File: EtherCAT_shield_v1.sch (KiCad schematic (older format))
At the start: 3 parts

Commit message: 配線
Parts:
- added C1: 0.1u, symbol C
- added C2, C3: 0.022u, symbol C
- added D1, D2: LED, symbol LED
- added P1: CONN_02X10, symbol CONN_02X10
- added P2, P3: CONN_02X19, symbol CONN_02X19
- added R1: 10k, symbol R
- added R2: 0R, symbol R
- added R3, R5: 330, symbol R
- added R4: 0, symbol R
- added R6, R7: R, symbol R
- gave numbers to parts that had none: 3
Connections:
- net labels added: +3V3, +5V
- wire segments 0 -> 146
- no-connect marks 1 -> 10
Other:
- moved on the sheet: J1, J2

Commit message: 部品修正．一度アノテーションとネットリスト生成
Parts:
- removed U1: LAN9252, symbol LAN9252
- added U1: LAN9252, Housings_DFN_QFN:QFN-64-1EP_9x9mm_Pitch0.5mm, symbol LAN9252
- C1, C2, C3: footprint (none) -> Capacitors_SMD:C_0603
- D1, D2: footprint (none) -> LEDs:LED_0603
- J1, J2: footprint (none) -> Connect:RJHSE538X
- P1: footprint (none) -> Socket_Strips:Socket_Strip_Straight_2x10_Pitch2.54mm
- P2, P3: footprint (none) -> Pin_Headers:Pin_Header_Straight_2x19_Pitch2.54mm
- R1: renamed from R6; footprint (none) -> Resistors_SMD:R_0603
- R2: renamed from R7; footprint (none) -> Resistors_SMD:R_0603
- R3: renamed from R2; footprint (none) -> Resistors_SMD:R_0603
- R4: renamed from R1; footprint (none) -> Resistors_SMD:R_0603
- R5: renamed from R3; footprint (none) -> Resistors_SMD:R_0603
- R6: renamed from R4; footprint (none) -> Resistors_SMD:R_0603
- R7: renamed from R5; footprint (none) -> Resistors_SMD:R_0603
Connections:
- wire segments 146 -> 138

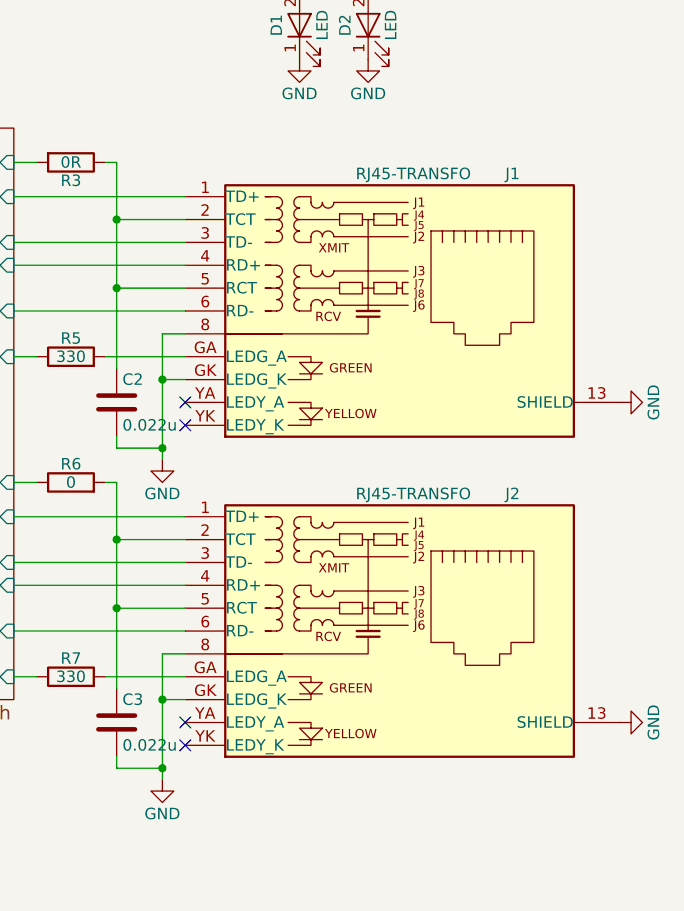
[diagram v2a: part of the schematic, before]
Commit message: 部品変更，再アノテーション，コネクタだけ配置
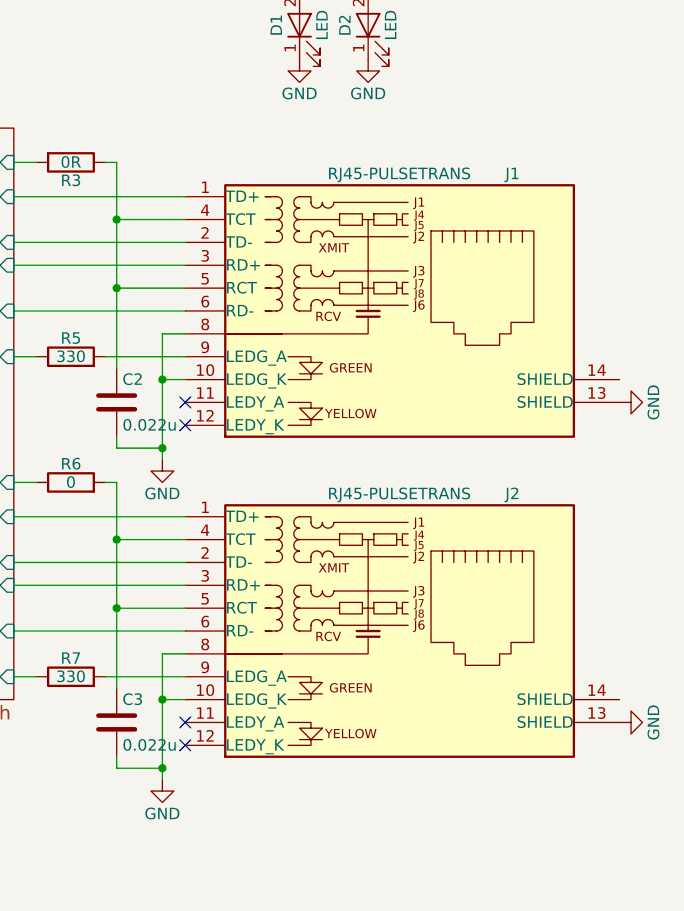
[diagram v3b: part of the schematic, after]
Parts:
- removed J1, J2: RJ45-TRANSFO, Connect:RJHSE538X, symbol RJ45-TRANSFO
- added J1, J2: RJ45-PULSETRANS, Connect:RJ45_J0011D21BNL, symbol RJ45-PULSETRANS
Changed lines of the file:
@@
 EESchema Schematic File Version 2
-LIBS:EtherCAT_shield_v1-rescue
 LIBS:power
 LIBS:device
@@
 $EndSheet
 $Comp
-L GND #PWR01
+L GND #PWR9
 U 1 1 58D8F78B
 P 10350 3150
-F 0 "#PWR01" H 10350 2900 50  0001 C CNN
+F 0 "#PWR9" H 10350 2900 50  0001 C CNN
 F 1 "GND" H 10350 3000 50  0000 C CNN
 F 2 "" H 10350 3150 50  0000 C CNN
@@
 $EndComp
 $Comp
-L GND #PWR02
+L GND #PWR13
 U 1 1 58D8F7A6
 P 10350 4550
-F 0 "#PWR02" H 10350 4300 50  0001 C CNN
+F 0 "#PWR13" H 10350 4300 50  0001 C CNN
 F 1 "GND" H 10350 4400 50  0000 C CNN
 F 2 "" H 10350 4550 50  0000 C CNN
@@
 	7700 2950 7800 2950
 $Comp
-L GND #PWR03
+L GND #PWR10
 U 1 1 58D9CD09
 P 8350 3400
-F 0 "#PWR03" H 8350 3150 50  0001 C CNN
+F 0 "#PWR10" H 8350 3150 50  0001 C CNN
 F 1 "GND" H 8350 3250 50  0000 C CNN
 F 2 "" H 8350 3400 50  0000 C CNN
@@
 Connection ~ 8350 4450
 $Comp
-L GND #PWR04
+L GND #PWR14
 U 1 1 58DAC772
 P 8350 4800
-F 0 "#PWR04" H 8350 4550 50  0001 C CNN
+F 0 "#PWR14" H 8350 4550 50  0001 C CNN
 F 1 "GND" H 8350 4650 50  0000 C CNN
 F 2 "" H 8350 4800 50  0000 C CNN
@@
 $EndComp
 $Comp
-L +3V3 #PWR05
+L +3V3 #PWR1
 U 1 1 58DDD983
 P 8950 1050
-F 0 "#PWR05" H 8950 900 50  0001 C CNN
+F 0 "#PWR1" H 8950 900 50  0001 C CNN
 F 1 "+3V3" H 8950 1190 50  0000 C CNN
 F 2 "" H 8950 1050 50  0000 C CNN
@@
 $EndComp
 $Comp
-L GND #PWR06
+L GND #PWR3
 U 1 1 58DDE236
 P 8950 1650
-F 0 "#PWR06" H 8950 1400 50  0001 C CNN
+F 0 "#PWR3" H 8950 1400 50  0001 C CNN
 F 1 "GND" H 8950 1500 50  0000 C CNN
 F 2 "" H 8950 1650 50  0000 C CNN
@@
 $EndComp
 $Comp
-L GND #PWR07
+L GND #PWR18
 U 1 1 58DE40E7
 P 3300 6100
-F 0 "#PWR07" H 3300 5850 50  0001 C CNN
+F 0 "#PWR18" H 3300 5850 50  0001 C CNN
 F 1 "GND" H 3300 5950 50  0000 C CNN
 F 2 "" H 3300 6100 50  0000 C CNN
@@
 $EndComp
 $Comp
-L GND #PWR08
+L GND #PWR15
 U 1 1 58DE4A0C
 P 3800 5500
-F 0 "#PWR08" H 3800 5250 50  0001 C CNN
+F 0 "#PWR15" H 3800 5250 50  0001 C CNN
 F 1 "GND" H 3800 5350 50  0000 C CNN
 F 2 "" H 3800 5500 50  0000 C CNN
@@
 $EndComp
 $Comp
-L GND #PWR09
+L GND #PWR19
 U 1 1 58DE5361
 P 3900 6100
-F 0 "#PWR09" H 3900 5850 50  0001 C CNN
+F 0 "#PWR19" H 3900 5850 50  0001 C CNN
 F 1 "GND" H 3900 5950 50  0000 C CNN
 F 2 "" H 3900 6100 50  0000 C CNN
@@
 Connection ~ 3850 6100
 $Comp
-L +3V3 #PWR010
+L +3V3 #PWR17
 U 1 1 58DE575E
 P 3950 5800
-F 0 "#PWR010" H 3950 5650 50  0001 C CNN
+F 0 "#PWR17" H 3950 5650 50  0001 C CNN
 F 1 "+3V3" H 3950 5940 50  0000 C CNN
 F 2 "" H 3950 5800 50  0000 C CNN
@@
 NoConn ~ 3300 5500
 $Comp
-L GND #PWR011
+L GND #PWR21
 U 1 1 58DE7D3E
 P 5950 6700
-F 0 "#PWR011" H 5950 6450 50  0001 C CNN
+F 0 "#PWR21" H 5950 6450 50  0001 C CNN
 F 1 "GND" H 5950 6550 50  0000 C CNN
 F 2 "" H 5950 6700 50  0000 C CNN
@@
 $EndComp
 $Comp
-L GND #PWR012
+L GND #PWR20
 U 1 1 58DE8701
 P 5950 6100
-F 0 "#PWR012" H 5950 5850 50  0001 C CNN
+F 0 "#PWR20" H 5950 5850 50  0001 C CNN
 F 1 "GND" H 5950 5950 50  0000 C CNN
 F 2 "" H 5950 6100 50  0000 C CNN
@@
 $EndComp
 $Comp
-L GND #PWR013
+L GND #PWR16
 U 1 1 58DE8FB1
 P 5450 5600
-F 0 "#PWR013" H 5450 5350 50  0001 C CNN
+F 0 "#PWR16" H 5450 5350 50  0001 C CNN
 F 1 "GND" H 5450 5450 50  0000 C CNN
 F 2 "" H 5450 5600 50  0000 C CNN
@@
 	2650 3300 2200 3300
 $Comp
-L GND #PWR014
+L GND #PWR12
 U 1 1 58DF79D7
 P 2200 3500
-F 0 "#PWR014" H 2200 3250 50  0001 C CNN
+F 0 "#PWR12" H 2200 3250 50  0001 C CNN
 F 1 "GND" H 2200 3350 50  0000 C CNN
 F 2 "" H 2200 3500 50  0000 C CNN
@@
 $EndComp
 $Comp
-L GND #PWR015
+L GND #PWR11
 U 1 1 58DF80F0
 P 1700 3500
-F 0 "#PWR015" H 1700 3250 50  0001 C CNN
+F 0 "#PWR11" H 1700 3250 50  0001 C CNN
 F 1 "GND" H 1700 3350 50  0000 C CNN
 F 2 "" H 1700 3500 50  0000 C CNN
@@
 	1650 2600 1650 2250
 $Comp
-L +3V3 #PWR016
+L +3V3 #PWR5
 U 1 1 58E0E7BC
 P 1650 2250
-F 0 "#PWR016" H 1650 2100 50  0001 C CNN
+F 0 "#PWR5" H 1650 2100 50  0001 C CNN
 F 1 "+3V3" H 1650 2390 50  0000 C CNN
 F 2 "" H 1650 2250 50  0000 C CNN
@@
 $EndComp
 $Comp
-L +5V #PWR017
+L +5V #PWR6
 U 1 1 58E0EC99
 P 2250 2250
-F 0 "#PWR017" H 2250 2100 50  0001 C CNN
+F 0 "#PWR6" H 2250 2100 50  0001 C CNN
 F 1 "+5V" H 2250 2390 50  0000 C CNN
 F 2 "" H 2250 2250 50  0000 C CNN
@@
 $EndComp
 $Comp
-L GND #PWR018
+L GND #PWR4
 U 1 1 58E0FDD7
 P 9250 1650
-F 0 "#PWR018" H 9250 1400 50  0001 C CNN
+F 0 "#PWR4" H 9250 1400 50  0001 C CNN
 F 1 "GND" H 9250 1500 50  0000 C CNN
 F 2 "" H 9250 1650 50  0000 C CNN
@@
 $EndComp
 $Comp
-L +5V #PWR019
+L +5V #PWR2
 U 1 1 58E10702
 P 9250 1050
-F 0 "#PWR019" H 9250 900 50  0001 C CNN
+F 0 "#PWR2" H 9250 900 50  0001 C CNN
 F 1 "+5V" H 9250 1190 50  0000 C CNN
 F 2 "" H 9250 1050 50  0000 C CNN
@@
 NoConn ~ 3300 4050
 $Comp
-L +3V3 #PWR020
+L +3V3 #PWR7
 U 1 1 58E1F1DF
 P 6500 2350
-F 0 "#PWR020" H 6500 2200 50  0001 C CNN
+F 0 "#PWR7" H 6500 2200 50  0001 C CNN
 F 1 "+3V3" H 6500 2490 50  0000 C CNN
 F 2 "" H 6500 2350 50  0000 C CNN
@@
 $EndComp
 $Comp
-L GND #PWR021
+L GND #PWR8
 U 1 1 58E20E63
 P 6500 3050
-F 0 "#PWR021" H 6500 2800 50  0001 C CNN
+F 0 "#PWR8" H 6500 2800 50  0001 C CNN
 F 1 "GND" H 6500 2900 50  0000 C CNN
 F 2 "" H 6500 3050 50  0000 C CNN
@@
 	3900 5800 3950 5800
 Connection ~ 3900 5800
-$Comp
-L RJ45-TRANSFO J1
-U 1 1 58D9E482
-P 9750 2750
-F 0 "J1" H 9850 3350 50  0000 L CNN
-F 1 "RJ45-TRANSFO" H 9700 3350 50  0000 R CNN
-F 2 "Connect:RJHSE538X" H 9750 2750 50  0001 C CNN
-F 3 "" H 9750 2750 50  0001 C CNN
-	1    9750 2750
-	1    0    0    -1
-$EndComp
-$Comp
-L RJ45-TRANSFO J2
-U 1 1 58D9F003
-P 9750 4150
-F 0 "J2" H 9850 4750 50  0000 L CNN
-F 1 "RJ45-TRANSFO" H 9700 4750 50  0000 R CNN
-F 2 "Connect:RJHSE538X" H 9750 4150 50  0001 C CNN
-F 3 "" H 9750 4150 50  0001 C CNN
-	1    9750 4150
-	1    0    0    -1
-$EndComp
 Wire Wire Line
 	8450 3750 8150 3750
@@
 	-1   0    0    -1
 $EndComp
+$Comp
+L RJ45-PULSETRANS J1
+U 1 1 58DA5610
+P 9750 2750
+F 0 "J1" H 9850 3350 50  0000 L CNN
+F 1 "RJ45-PULSETRANS" H 9700 3350 50  0000 R CNN
+F 2 "Connect:RJ45_J0011D21BNL" H 9750 2750 50  0001 C CNN
+F 3 "" H 9750 2750 50  0001 C CNN
+	1    9750 2750
+	1    0    0    -1
+$EndComp
+$Comp
+L RJ45-PULSETRANS J2
+U 1 1 58DA58D5
+P 9750 4150
+F 0 "J2" H 9850 4750 50  0000 L CNN
+F 1 "RJ45-PULSETRANS" H 9700 4750 50  0000 R CNN
+F 2 "Connect:RJ45_J0011D21BNL" H 9750 4150 50  0001 C CNN
+F 3 "" H 9750 4150 50  0001 C CNN
+	1    9750 4150
+	1    0    0    -1
+$EndComp
 $EndSCHEMATC

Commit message: 進捗
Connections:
- net labels added: RX1_N, RX1_P, RX2_N, RX2_P, TX1_N, TX1_P, TX2_N, TX2_P
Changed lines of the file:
@@
 $EndSheet
 $Comp
-L GND #PWR9
+L GND #PWR01
 U 1 1 58D8F78B
 P 10350 3150
-F 0 "#PWR9" H 10350 2900 50  0001 C CNN
+F 0 "#PWR01" H 10350 2900 50  0001 C CNN
 F 1 "GND" H 10350 3000 50  0000 C CNN
 F 2 "" H 10350 3150 50  0000 C CNN
@@
 $EndComp
 $Comp
-L GND #PWR13
+L GND #PWR02
 U 1 1 58D8F7A6
 P 10350 4550
-F 0 "#PWR13" H 10350 4300 50  0001 C CNN
+F 0 "#PWR02" H 10350 4300 50  0001 C CNN
 F 1 "GND" H 10350 4400 50  0000 C CNN
 F 2 "" H 10350 4550 50  0000 C CNN
@@
 	7700 2950 7800 2950
 $Comp
-L GND #PWR10
+L GND #PWR03
 U 1 1 58D9CD09
 P 8350 3400
-F 0 "#PWR10" H 8350 3150 50  0001 C CNN
+F 0 "#PWR03" H 8350 3150 50  0001 C CNN
 F 1 "GND" H 8350 3250 50  0000 C CNN
 F 2 "" H 8350 3400 50  0000 C CNN
@@
 Connection ~ 8350 4450
 $Comp
-L GND #PWR14
+L GND #PWR04
 U 1 1 58DAC772
 P 8350 4800
-F 0 "#PWR14" H 8350 4550 50  0001 C CNN
+F 0 "#PWR04" H 8350 4550 50  0001 C CNN
 F 1 "GND" H 8350 4650 50  0000 C CNN
 F 2 "" H 8350 4800 50  0000 C CNN
@@
 $EndComp
 $Comp
-L +3V3 #PWR1
+L +3V3 #PWR05
 U 1 1 58DDD983
 P 8950 1050
-F 0 "#PWR1" H 8950 900 50  0001 C CNN
+F 0 "#PWR05" H 8950 900 50  0001 C CNN
 F 1 "+3V3" H 8950 1190 50  0000 C CNN
 F 2 "" H 8950 1050 50  0000 C CNN
@@
 $EndComp
 $Comp
-L GND #PWR3
+L GND #PWR06
 U 1 1 58DDE236
 P 8950 1650
-F 0 "#PWR3" H 8950 1400 50  0001 C CNN
+F 0 "#PWR06" H 8950 1400 50  0001 C CNN
 F 1 "GND" H 8950 1500 50  0000 C CNN
 F 2 "" H 8950 1650 50  0000 C CNN
@@
 $EndComp
 $Comp
-L GND #PWR18
+L GND #PWR07
 U 1 1 58DE40E7
 P 3300 6100
-F 0 "#PWR18" H 3300 5850 50  0001 C CNN
+F 0 "#PWR07" H 3300 5850 50  0001 C CNN
 F 1 "GND" H 3300 5950 50  0000 C CNN
 F 2 "" H 3300 6100 50  0000 C CNN
@@
 $EndComp
 $Comp
-L GND #PWR15
+L GND #PWR08
 U 1 1 58DE4A0C
 P 3800 5500
-F 0 "#PWR15" H 3800 5250 50  0001 C CNN
+F 0 "#PWR08" H 3800 5250 50  0001 C CNN
 F 1 "GND" H 3800 5350 50  0000 C CNN
 F 2 "" H 3800 5500 50  0000 C CNN
@@
 $EndComp
 $Comp
-L GND #PWR19
+L GND #PWR09
 U 1 1 58DE5361
 P 3900 6100
-F 0 "#PWR19" H 3900 5850 50  0001 C CNN
+F 0 "#PWR09" H 3900 5850 50  0001 C CNN
 F 1 "GND" H 3900 5950 50  0000 C CNN
 F 2 "" H 3900 6100 50  0000 C CNN
@@
 Connection ~ 3850 6100
 $Comp
-L +3V3 #PWR17
+L +3V3 #PWR010
 U 1 1 58DE575E
 P 3950 5800
-F 0 "#PWR17" H 3950 5650 50  0001 C CNN
+F 0 "#PWR010" H 3950 5650 50  0001 C CNN
 F 1 "+3V3" H 3950 5940 50  0000 C CNN
 F 2 "" H 3950 5800 50  0000 C CNN
@@
 NoConn ~ 3300 5500
 $Comp
-L GND #PWR21
+L GND #PWR011
 U 1 1 58DE7D3E
 P 5950 6700
-F 0 "#PWR21" H 5950 6450 50  0001 C CNN
+F 0 "#PWR011" H 5950 6450 50  0001 C CNN
 F 1 "GND" H 5950 6550 50  0000 C CNN
 F 2 "" H 5950 6700 50  0000 C CNN
@@
 $EndComp
 $Comp
-L GND #PWR20
+L GND #PWR012
 U 1 1 58DE8701
 P 5950 6100
-F 0 "#PWR20" H 5950 5850 50  0001 C CNN
+F 0 "#PWR012" H 5950 5850 50  0001 C CNN
 F 1 "GND" H 5950 5950 50  0000 C CNN
 F 2 "" H 5950 6100 50  0000 C CNN
@@
 $EndComp
 $Comp
-L GND #PWR16
+L GND #PWR013
 U 1 1 58DE8FB1
 P 5450 5600
-F 0 "#PWR16" H 5450 5350 50  0001 C CNN
+F 0 "#PWR013" H 5450 5350 50  0001 C CNN
 F 1 "GND" H 5450 5450 50  0000 C CNN
 F 2 "" H 5450 5600 50  0000 C CNN
@@
 	2650 3300 2200 3300
 $Comp
-L GND #PWR12
+L GND #PWR014
 U 1 1 58DF79D7
 P 2200 3500
-F 0 "#PWR12" H 2200 3250 50  0001 C CNN
+F 0 "#PWR014" H 2200 3250 50  0001 C CNN
 F 1 "GND" H 2200 3350 50  0000 C CNN
 F 2 "" H 2200 3500 50  0000 C CNN
@@
 $EndComp
 $Comp
-L GND #PWR11
+L GND #PWR015
 U 1 1 58DF80F0
 P 1700 3500
-F 0 "#PWR11" H 1700 3250 50  0001 C CNN
+F 0 "#PWR015" H 1700 3250 50  0001 C CNN
 F 1 "GND" H 1700 3350 50  0000 C CNN
 F 2 "" H 1700 3500 50  0000 C CNN
@@
 	1650 2600 1650 2250
 $Comp
-L +3V3 #PWR5
+L +3V3 #PWR016
 U 1 1 58E0E7BC
 P 1650 2250
-F 0 "#PWR5" H 1650 2100 50  0001 C CNN
+F 0 "#PWR016" H 1650 2100 50  0001 C CNN
 F 1 "+3V3" H 1650 2390 50  0000 C CNN
 F 2 "" H 1650 2250 50  0000 C CNN
@@
 $EndComp
 $Comp
-L +5V #PWR6
+L +5V #PWR017
 U 1 1 58E0EC99
 P 2250 2250
-F 0 "#PWR6" H 2250 2100 50  0001 C CNN
+F 0 "#PWR017" H 2250 2100 50  0001 C CNN
 F 1 "+5V" H 2250 2390 50  0000 C CNN
 F 2 "" H 2250 2250 50  0000 C CNN
@@
 $EndComp
 $Comp
-L GND #PWR4
+L GND #PWR018
 U 1 1 58E0FDD7
 P 9250 1650
-F 0 "#PWR4" H 9250 1400 50  0001 C CNN
+F 0 "#PWR018" H 9250 1400 50  0001 C CNN
 F 1 "GND" H 9250 1500 50  0000 C CNN
 F 2 "" H 9250 1650 50  0000 C CNN
@@
 $EndComp
 $Comp
-L +5V #PWR2
+L +5V #PWR019
 U 1 1 58E10702
 P 9250 1050
-F 0 "#PWR2" H 9250 900 50  0001 C CNN
+F 0 "#PWR019" H 9250 900 50  0001 C CNN
 F 1 "+5V" H 9250 1190 50  0000 C CNN
 F 2 "" H 9250 1050 50  0000 C CNN
@@
 NoConn ~ 3300 4050
 $Comp
-L +3V3 #PWR7
+L +3V3 #PWR020
 U 1 1 58E1F1DF
 P 6500 2350
-F 0 "#PWR7" H 6500 2200 50  0001 C CNN
+F 0 "#PWR020" H 6500 2200 50  0001 C CNN
 F 1 "+3V3" H 6500 2490 50  0000 C CNN
 F 2 "" H 6500 2350 50  0000 C CNN
@@
 $EndComp
 $Comp
-L GND #PWR8
+L GND #PWR021
 U 1 1 58E20E63
 P 6500 3050
-F 0 "#PWR8" H 6500 2800 50  0001 C CNN
+F 0 "#PWR021" H 6500 2800 50  0001 C CNN
 F 1 "GND" H 6500 2900 50  0000 C CNN
 F 2 "" H 6500 3050 50  0000 C CNN
@@
 	1    0    0    -1
 $EndComp
+Text GLabel 8250 2250 1    60   Input ~ 0
+TX1_P
+Text GLabel 8350 2450 1    60   Input ~ 0
+TX1_N
+Text GLabel 7950 2550 1    60   Input ~ 0
+RX1_P
+Text GLabel 8050 2750 1    60   Input ~ 0
+RX1_N
+Text GLabel 8250 3650 1    60   Input ~ 0
+TX2_P
+Text GLabel 8350 3850 1    60   Input ~ 0
+TX2_N
+Text GLabel 7900 3950 1    60   Input ~ 0
+RX2_P
+Text GLabel 8000 4150 1    60   Input ~ 0
+RX2_N
 $EndSCHEMATC

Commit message: 進捗
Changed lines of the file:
@@
 Text GLabel 8000 4150 1    60   Input ~ 0
 RX2_N
+$Comp
+L GND #PWR022
+U 1 1 58DB51B6
+P 10350 3050
+F 0 "#PWR022" H 10350 2800 50  0001 C CNN
+F 1 "GND" H 10350 2900 50  0000 C CNN
+F 2 "" H 10350 3050 50  0000 C CNN
+F 3 "" H 10350 3050 50  0000 C CNN
+	1    10350 3050
+	0    -1   -1   0
+$EndComp
+$Comp
+L GND #PWR023
+U 1 1 58DB58F4
+P 10350 4450
+F 0 "#PWR023" H 10350 4200 50  0001 C CNN
+F 1 "GND" H 10350 4300 50  0000 C CNN
+F 2 "" H 10350 4450 50  0000 C CNN
+F 3 "" H 10350 4450 50  0000 C CNN
+	1    10350 4450
+	0    -1   -1   0
+$EndComp
 $EndSCHEMATC

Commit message: 進捗
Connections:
- net labels added: GNDPWR
- wire segments 138 -> 151

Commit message: 進捗
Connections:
- net +5V: now also P2.6 (P6)
- net LAN9252/IRQ: now also P2.21 (P21)
- net at U1.18 (SYNC1/LATCH1): now also P2.27 (P27)
- net at U1.34 (SYNC0/LATCH0): now also P2.25 (P25)
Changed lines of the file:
@@
 	6950 3300 5000 3300
 Wire Wire Line
-	5000 3300 5000 4100
+	5000 3300 5000 4900
 Wire Wire Line
 	4450 3000 4800 3000
 Wire Wire Line
-	4800 3000 4800 4100
+	4800 3000 4800 4750
 Wire Wire Line
 	4450 2900 4900 2900
 Wire Wire Line
-	4900 2900 4900 4100
+	4900 2900 4900 4800
 Wire Wire Line
 	6800 3150 6800 2700
@@
 Wire Wire Line
 	2700 6300 3300 6300
+Wire Wire Line
+	5000 4900 2400 4900
+Wire Wire Line
+	2400 4900 2400 6200
+Wire Wire Line
+	2400 6200 3300 6200
+Wire Wire Line
+	4800 4750 2300 4750
+Wire Wire Line
+	2300 4750 2300 6400
+Wire Wire Line
+	2300 6400 3300 6400
+Wire Wire Line
+	4900 4800 2200 4800
+Wire Wire Line
+	2200 4800 2200 6500
+Wire Wire Line
+	2200 6500 3300 6500
+$Comp
+L +5V #PWR?
+U 1 1 58DD1482
+P 3800 5400
+F 0 "#PWR?" H 3800 5250 50  0001 C CNN
+F 1 "+5V" H 3800 5540 50  0000 C CNN
+F 2 "" H 3800 5400 50  0001 C CNN
+F 3 "" H 3800 5400 50  0001 C CNN
+	1    3800 5400
+	0    1    1    0
+$EndComp
 $EndSCHEMATC
